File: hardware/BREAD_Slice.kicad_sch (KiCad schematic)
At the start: 60 parts, among them IC1 ADS131M08IPBS, J1 Conn_01x10_Female, J2 Screw_Term_01x04, J3 Screw_Term_01x04, J4 Screw_Term_01x04, J5 Screw_Term_01x04, J6 Screw_Term_01x04, J7 Screw_Term_01x04, J8 Screw_Term_01x04, J9 Screw_Term_01x04, U1 AP63205, U2 OP1177ARM, Y1 ACO-xxxMHz

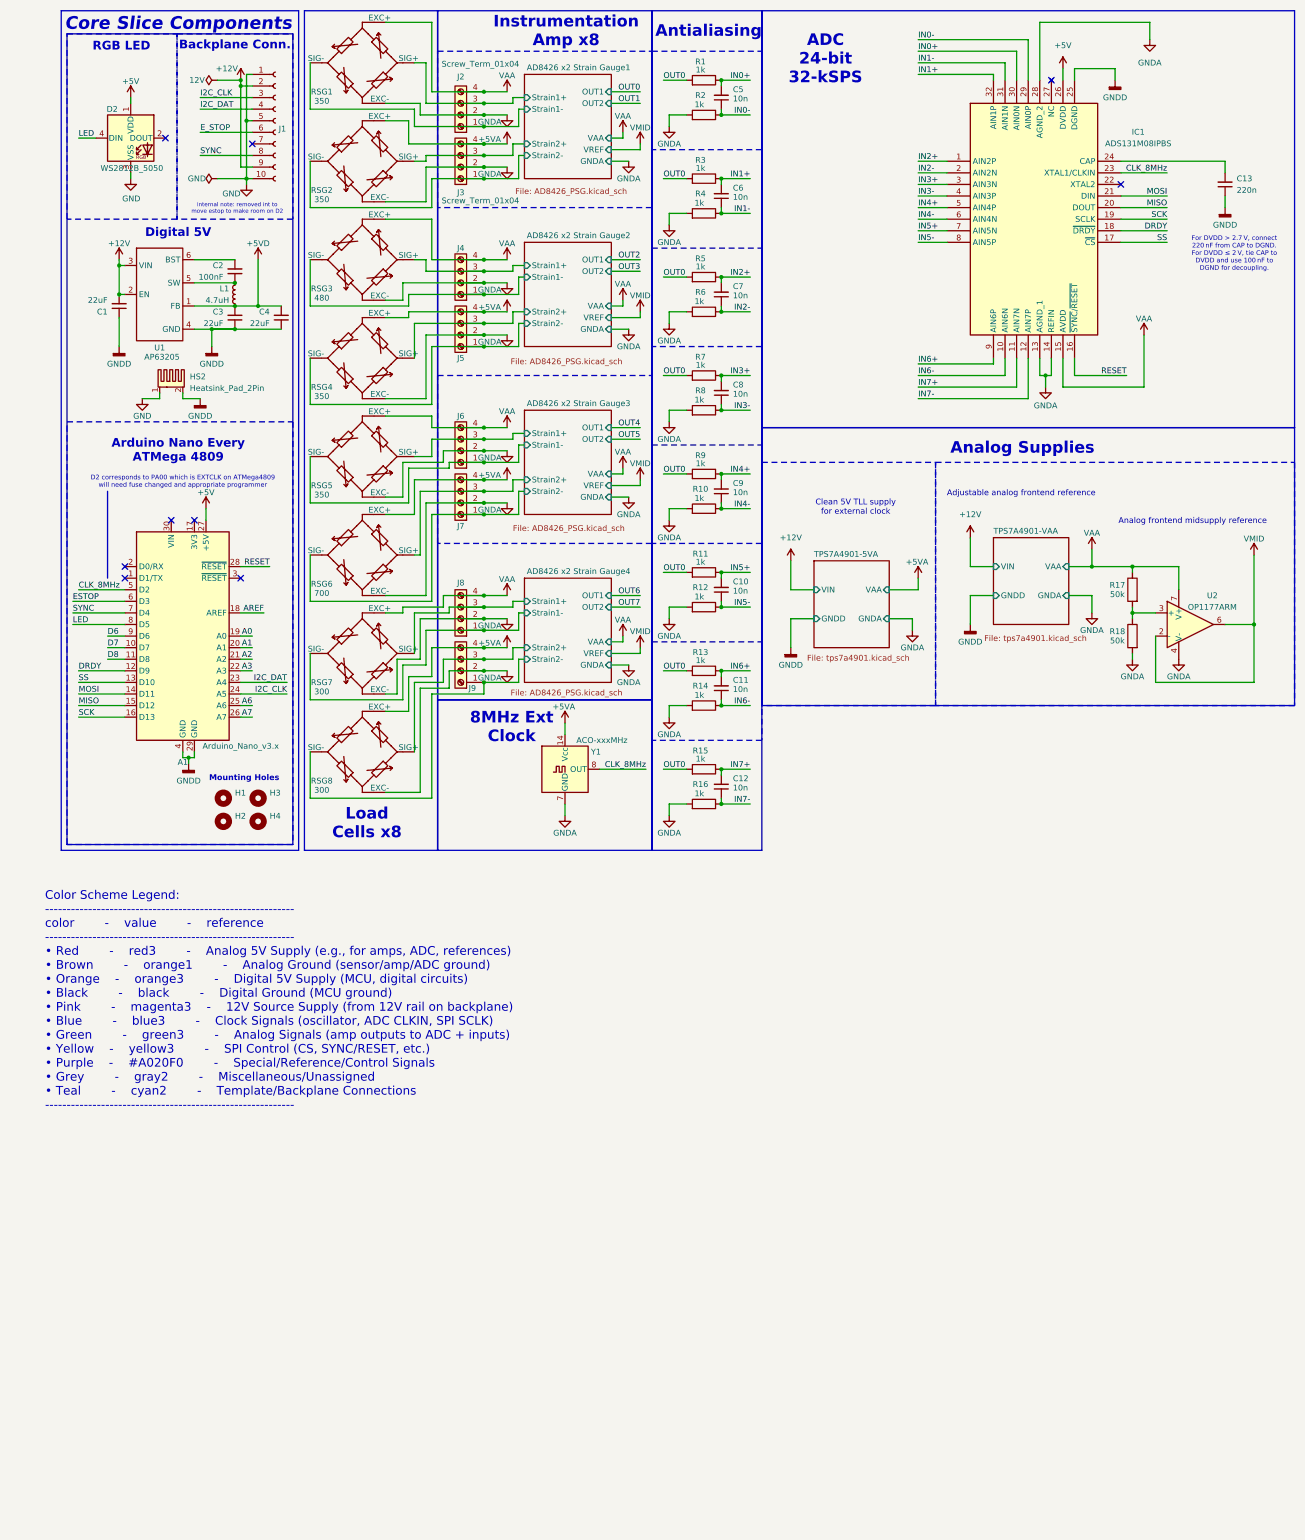
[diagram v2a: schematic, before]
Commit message: finalize board before switch to stm
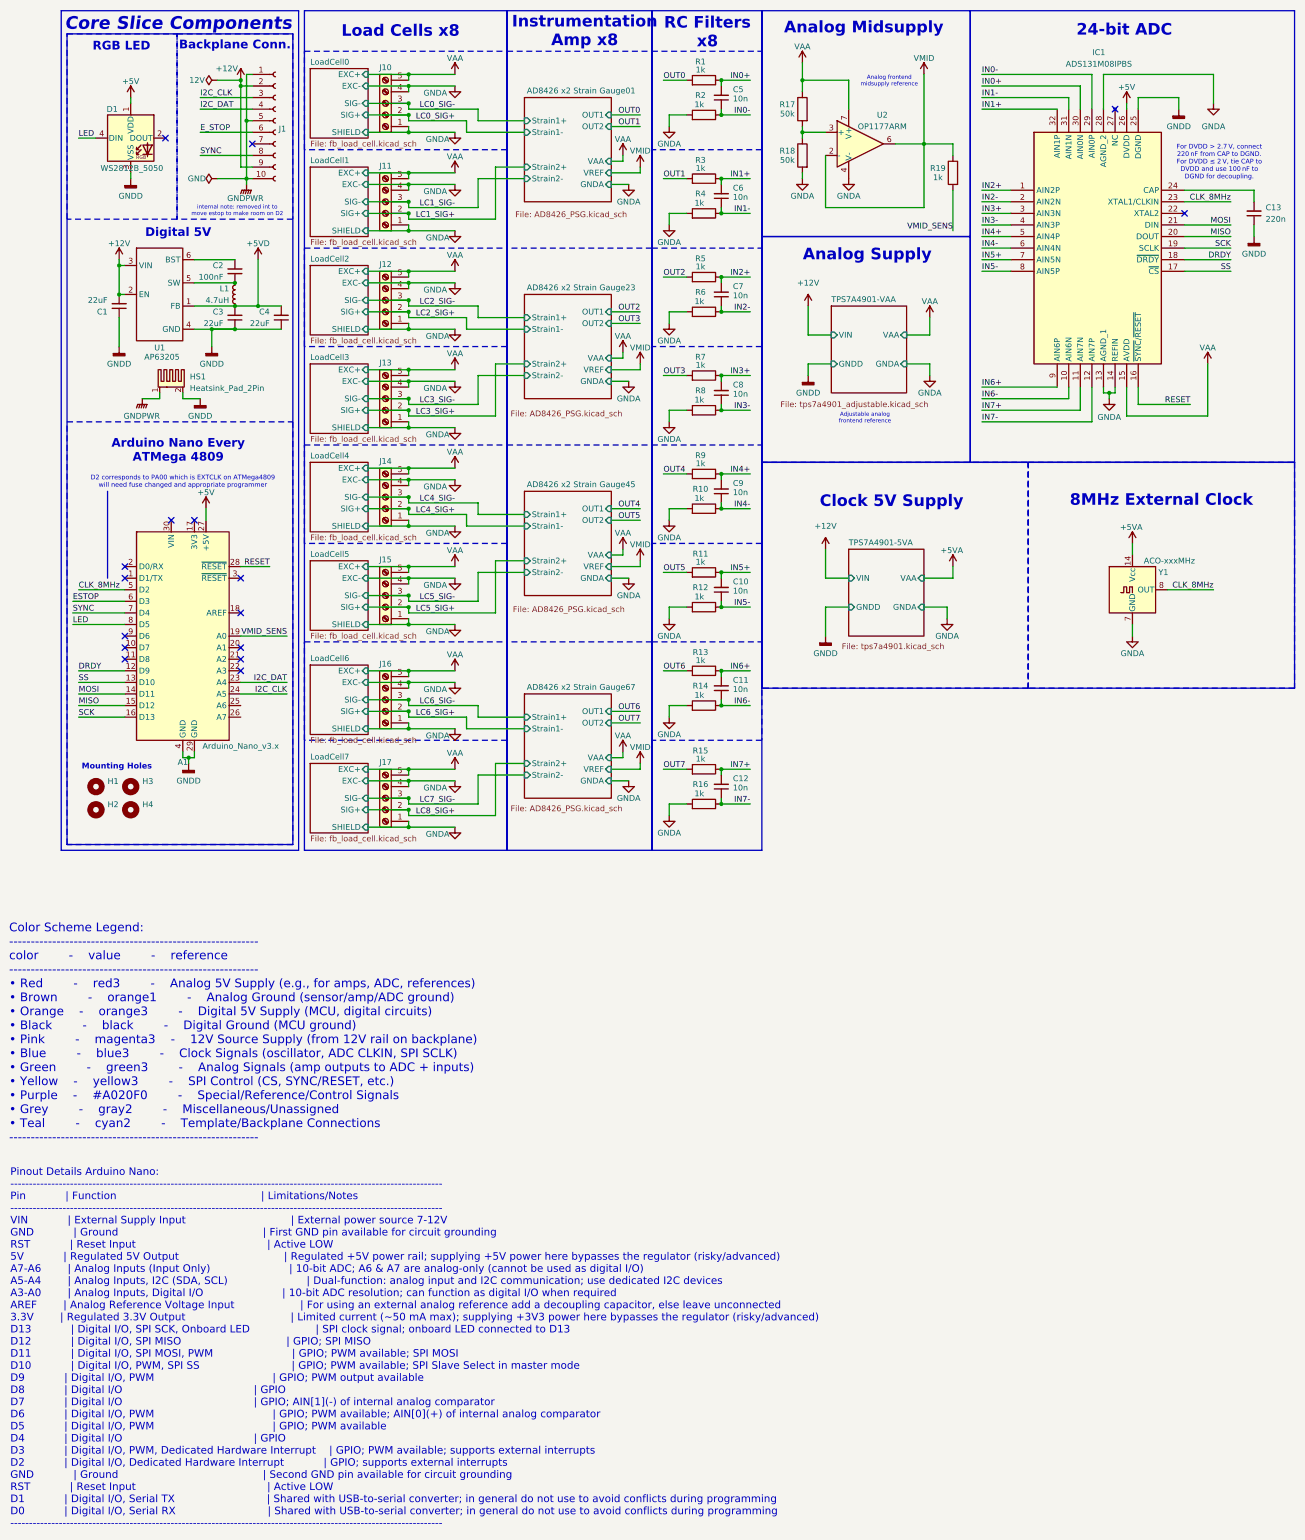
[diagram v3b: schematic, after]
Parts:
- removed J2, J3, J4, J5, J6, J7, J8, J9: Screw_Term_01x04, symbol Connector:Screw_Terminal_01x04
- removed RSG1, RSG2, RSG4, RSG5: 350, symbol kml-custom:Full Bridge Strain Gauge
- removed RSG3: 480, symbol kml-custom:Full Bridge Strain Gauge
- removed RSG6: 700, symbol kml-custom:Full Bridge Strain Gauge
- removed RSG7, RSG8: 300, symbol kml-custom:Full Bridge Strain Gauge
- added J10, J11, J12, J13, J14, J15, J16, J17: Screw_Terminal_01x05, TerminalBlock_4Ucon:TerminalBlock_4Ucon_1x05_P3.50mm_Horizontal, symbol Connector:Screw_Terminal_01x05
- added R19: 1k, symbol Device:R
- renumbered D2 to D1, HS2 to HS1
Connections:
- net GNDA: now also J10.1 (Pin_1), J10.4 (Pin_4), J11.1 (Pin_1), J11.4 (Pin_4), J12.1 (Pin_1), J12.4 (Pin_4), J13.1 (Pin_1), J13.4 (Pin_4), J14.1 (Pin_1), J14.4 (Pin_4), J15.1 (Pin_1), J15.4 (Pin_4), J16.1 (Pin_1), J16.4 (Pin_4), J17.1 (Pin_1), J17.4 (Pin_4)
- net GNDD: now also D1.3 (VSS)
- net OUT0: no longer R11.2, R13.2, R15.2, R3.2, R5.2, R7.2, R9.2
- net OUT1: now also R3.2
- net OUT2: now also R5.2
- net OUT3: now also R7.2
- net OUT4: now also R9.2
- net OUT5: now also R11.2
- net OUT6: now also R13.2
- net OUT7: now also R15.2
- net VAA: now also J10.5 (Pin_5), J11.5 (Pin_5), J12.5 (Pin_5), J13.5 (Pin_5), J14.5 (Pin_5), J15.5 (Pin_5), J16.5 (Pin_5), J17.5 (Pin_5)
- net VMID: now also R19.1
- net A0 renamed VMID_SENS
- net VMID_SENS: now also R19.2
- net A1: no longer names the net of A1.20 (A1)
- net A2: no longer names the net of A1.21 (A2)
- net A3: no longer names the net of A1.22 (A3)
- net A6: no longer names the net of A1.25 (A6)
- net A7: no longer names the net of A1.26 (A7)
- net AREF: no longer names the net of A1.18 (AREF)
- net D6: no longer names the net of A1.9 (D6)
- net D7: no longer names the net of A1.10 (D7)
- net D8: no longer names the net of A1.11 (D8)
- net GND renamed GNDPWR
- net GNDPWR: no longer D1.3 (VSS)
- new net LC0_SIG+: J10.2 (Pin_2)
- new net LC0_SIG-: J10.3 (Pin_3)
- new net LC1_SIG+: J11.2 (Pin_2)
- new net LC1_SIG-: J11.3 (Pin_3)
- new net LC2_SIG+: J12.2 (Pin_2)
- new net LC2_SIG-: J12.3 (Pin_3)
- new net LC3_SIG+: J13.2 (Pin_2)
- new net LC3_SIG-: J13.3 (Pin_3)
- new net LC4_SIG+: J14.2 (Pin_2)
- new net LC4_SIG-: J14.3 (Pin_3)
- new net LC5_SIG+: J15.2 (Pin_2)
- new net LC5_SIG-: J15.3 (Pin_3)
- new net LC6_SIG+: J16.2 (Pin_2)
- new net LC6_SIG-: J16.3 (Pin_3)
- new net LC7_SIG-: J17.3 (Pin_3)
- new net LC8_SIG+: J17.2 (Pin_2)
- no-connect marks 9 -> 16
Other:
- sheet AD8426 x2 Strain Gauge1 renamed AD8426 x2 Strain Gauge01
- sheet AD8426 x2 Strain Gauge2 renamed AD8426 x2 Strain Gauge23
- sheet AD8426 x2 Strain Gauge3 renamed AD8426 x2 Strain Gauge45
- sheet AD8426 x2 Strain Gauge4 renamed AD8426 x2 Strain Gauge67
- added sheet LoadCell0 (fb_load_cell.kicad_sch)
- added sheet LoadCell1 (fb_load_cell.kicad_sch)
- added sheet LoadCell2 (fb_load_cell.kicad_sch)
- added sheet LoadCell3 (fb_load_cell.kicad_sch)
- added sheet LoadCell4 (fb_load_cell.kicad_sch)
- added sheet LoadCell5 (fb_load_cell.kicad_sch)
- added sheet LoadCell6 (fb_load_cell.kicad_sch)
- added sheet LoadCell7 (fb_load_cell.kicad_sch)
- sheet TPS7A4901-VAA: file tps7a4901.kicad_sch -> tps7a4901_adjustable.kicad_sch
- note added: "24-bit ADC"
- note added: "8MHz External Clock"
- note added: "Analog Midsupply"
- note added: "Analog Supply"
- note added: "Clock 5V Supply"
- note added: "Pinout Details Arduino Nano: -------------------------------------------------------------------------------------------------------------------- Pin | Function | Limitations/Notes -------------------------------------------------------------------------------------------------------------------- VIN | External Supply Input | External power source 7-12V GND | Ground | First GND pin available for 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"
- note added: "RC Filters x8"
- note removed: "8MHz Ext Clock"
- note removed: "ADC 24-bit 32-kSPS"
- note removed: "Analog Supplies"
- note removed: "Antialiasing"
- note removed: "Clean 5V TLL supply for external clock"
- moved on the sheet: C13, H1, H2, H3, H4, IC1, R17, R18, U2, Y1

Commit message: final iteration of board with proper connectors and clean layout
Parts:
- removed A1: Arduino_Nano_v3.x, Module:Arduino_Nano, symbol MCU_Module:Arduino_Nano_v3.x
- removed HS1: Heatsink_Pad_2Pin, symbol Mechanical:Heatsink_Pad_2Pin
- removed J10, J11, J12, J13, J14, J15, J16, J17: Screw_Terminal_01x05, TerminalBlock_4Ucon:TerminalBlock_4Ucon_1x05_P3.50mm_Horizontal, symbol Connector:Screw_Terminal_01x05
- removed U2: OP1177ARM, Package_SO:MSOP-8_3x3mm_P0.65mm, symbol Amplifier_Operational:OP1177ARM
- removed Y1: ACO-xxxMHz, Oscillator:Oscillator_DIP-14, symbol Oscillator:ACO-xxxMHz
- added C13, C14: 1u, Capacitor_SMD:C_1206_3216Metric_Pad1.33x1.80mm_HandSolder, symbol Device:C_Small
- added HS1: Heatsink_Pad, kml-custom:Thermal Pad, symbol Mechanical:Heatsink_Pad
- added J10: Micro_SD_Card, Connector_Card:microSD_HC_Molex_47219-2001, symbol Connector:Micro_SD_Card
- added J2, J3, J4, J5, J6, J7, J8, J9: 1439890, 1439890, symbol kml-custom:1439890
- added NT1: NetTie_2, NetTie:NetTie-2_SMD_Pad2.0mm, symbol Device:NetTie_2
- added R20: 1k, Resistor_SMD:R_0805_2012Metric_Pad1.20x1.40mm_HandSolder, symbol Device:R
- added U2: NUCLEO-L432KC, kml-custom:MODULE_NUCLEO-L432KC, symbol kml-custom:NUCLEO-L432KC
- added U3: MCP6022, Package_SO:SOIC-8_3.9x4.9mm_P1.27mm, symbol Amplifier_Operational:MCP6022
- C10, C11, C12, C5, C6, C7, C8, C9: footprint Capacitor_SMD:C_1206_3216Metric -> Capacitor_SMD:C_0805_2012Metric_Pad1.18x1.45mm_HandSolder
- C15: renamed from C13; footprint Capacitor_SMD:C_1206_3216Metric -> Capacitor_SMD:C_1206_3216Metric_Pad1.33x1.80mm_HandSolder
- D1: footprint SparkFun-LED:WS2812-5050-4pin -> SparkFun-LED:WS2812-5050-4PIN
- IC1: footprint QFP50P700X700X120-32N -> kml-custom:QFP50P700X700X120-32N
- R1, R10, R11, R12, R13, R14, R15, R16, R19, R2, R3, R4, R5, R6, R7, R8, R9: footprint (none) -> Resistor_SMD:R_0805_2012Metric_Pad1.20x1.40mm_HandSolder
- R17, R18: value 50k -> 50k 1%; footprint (none) -> Resistor_SMD:R_0805_2012Metric_Pad1.20x1.40mm_HandSolder
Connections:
- net E_STOP is gone; now on net ESTOP: J1.6 (Pin_6)
- net +5VD: now also D1.1 (VDD), U2.CN4_4 (+5V), U3.8 (V+)
- net DRDY: now also U2.CN3_11 (PC15)
- net ESTOP: now also U2.CN3_5 (PA12)
- net GNDA: now also C14.1, J2.4, J2.5, J2.6, J3.4, J3.5, J3.6, J4.4, J4.5, J4.6, J5.4, J5.5, J5.6, J6.3, J6.5, J6.6, J7.3, J7.5, J7.6, J8.3, J8.5, J8.6, J9.3, J9.5, J9.6
- net GNDD: now also C13.1, HS1.1, J10.6 (VSS), J10.9 (SHIELD), NT1.2, U2.CN3_4 (GND_CN3), U2.CN4_2 (GND_CN4), U3.4 (V-)
- net GNDPWR: now also NT1.1
- net I2C_CLK: now also U2.CN4_7 (PA6)
- net I2C_DAT: now also U2.CN4_8 (PA5)
- net IN0+: now also IC1.29 (AIN0P); no longer IC1.30 (AIN0N)
- net IN0-: now also IC1.30 (AIN0N); no longer IC1.29 (AIN0P)
- net IN3+: now also IC1.4 (AIN3P); no longer IC1.3 (AIN3N)
- net IN3-: now also IC1.3 (AIN3N); no longer IC1.4 (AIN3P)
- net IN5+: now also IC1.8 (AIN5P); no longer IC1.7 (AIN5N)
- net IN5-: now also IC1.7 (AIN5N); no longer IC1.8 (AIN5P)
- net IN7+: now also IC1.12 (AIN7P); no longer IC1.11 (AIN7N)
- net IN7-: now also IC1.11 (AIN7N); no longer IC1.12 (AIN7P)
- net LC0_SIG+: now also J6.1
- net LC0_SIG-: now also J6.2
- net LC1_SIG+: now also J2.2
- net LC1_SIG-: now also J2.1
- net LC2_SIG+: now also J7.1
- net LC2_SIG-: now also J7.2
- net LC3_SIG+: now also J3.2
- net LC3_SIG-: now also J3.1
- net LC4_SIG+: now also J8.1
- net LC4_SIG-: now also J8.2
- net LC5_SIG+: now also J4.2
- net LC5_SIG-: now also J4.1
- net LC6_SIG+: now also J9.1
- net LC6_SIG-: now also J9.2
- net LC7_SIG-: now also J5.1
- net LED: now also U2.CN3_8 (PB6)
- net MISO: now also J10.7 (DAT0), U2.CN3_15 (PB4)
- net MOSI: now also J10.3 (CMD), U2.CN3_14 (PB5)
- net SCK: now also J10.5 (CLK), U2.CN4_15 (PB3)
- net SYNC: now also U2.CN3_7 (PB7)
- net VAA: now also J2.3, J3.3, J4.3, J5.3, J6.4, J7.4, J8.4, J9.4; no longer IC1.15 (AVDD)
- net VMID: now also U3.1, U3.2 (-)
- net VMID_SENS: now also U2.CN4_12 (PA0)
- net INT: now reaches J1.7 (Pin_7)
- net INT: now also U2.CN3_6 (PB0)
- net at R17.2, R18.1: now also U3.3 (+)
- net +5V renamed +3V3
- net +3V3: now also C13.2, J10.4 (VDD), U2.CN4_14 (+3V3); no longer D1.1 (VDD)
- net CLK_8MHz renamed CLK_MCO
- net CLK_MCO: now also U2.CN3_12 (PA8)
- net RESET renamed RST_ADC
- net RST_ADC: now also U2.CN3_10 (PC14)
- net SS renamed ADC_CS
- net ADC_CS: now also U2.CN3_9 (PB1)
- new net: R20.1, U3.6 (-), U3.7
- new net +3.3VADC: C14.2, IC1.15 (AVDD), U3.5 (+)
- new net LC7_SIG+: J5.2
- new net SD_CS: J10.2 (DAT3/CD), U2.CN3_13 (PA11)
- new net VADC_SENS: R20.2, U2.CN4_11 (PA1)
- no-connect marks 16 -> 20
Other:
- sheet AD8426 x2 Strain Gauge01 renamed AD8426 x2 StrainGauge01
- sheet AD8426 x2 Strain Gauge23 renamed AD8426 x2 StrainGauge23
- sheet AD8426 x2 Strain Gauge45 renamed AD8426 x2 StrainGauge45
- sheet AD8426 x2 Strain Gauge67 renamed AD8426 x2 StrainGauge67
- sheet TPS7A4901-5VA renamed TPS7A4901-3V3ADC
- sheet TPS7A4901-3V3ADC ports: added GND; removed GNDD
- sheet TPS7A4901-VAA ports: added GND; removed GNDD
- note added: "ADC 3V3 Supply"
- note added: "ADC Supply Sense Buffer"
- note added: "Analog Frontend 5-10V Supply"
- note added: "Analog Midsupply Reference"
- note added: "M12 Connectors"
- note added: "Pinout Details: STM32 Nucleo-32 L432KC ------------------------------------------------------------------------------------- Pin | Function | Notes ------------------------------------------------------------------------------------- VIN | External Supply Input | 7-12V input via CN4 pin 1; powers onboard 3.3V regulator GND | Ground | Ground reference (multiple available) NRST | Reset Input | Acti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"
- note added: "SB10 (VREF+) - ON: VREF+ on STM32 is connected to VDD. - OFF: VREF+ on STM32 is not connected to VDD and it is provided by pin 13 of CN4. SB15 (LD3-LED) - ON: Green user LED LD3 is connected to D13 of ARDUINO® Nano signal. - OFF: Green user LED LD3 is not connected. SB9 (NRST) - ON: The NRST signal of ST-LINK is connected to the NRST pin of the STM32. - OFF: The NRST signal of ST-LINK is not conn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"
- note added: "STM32 NUCLEO32 STM32L432KC"
- note removed: "8MHz External Clock"
- note removed: "Adjustable analog frontend reference"
- note removed: "Analog Midsupply"
- note removed: "Analog Supply"
- note removed: "Analog frontend midsupply reference"
- note removed: "Arduino Nano Every ATMega 4809"
- note removed: "Clock 5V Supply"
- note removed: "D2 corresponds to PA00 which is EXTCLK on ATMega4809 will need fuse changed and appropriate programmer"
- note removed: "Pinout Details Arduino Nano: -------------------------------------------------------------------------------------------------------------------- Pin | Function | Limitations/Notes -------------------------------------------------------------------------------------------------------------------- VIN | External Supply Input | External power source 7-12V GND | Ground | First GND pin available for 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"
- moved on the sheet: C10, C11, C12, C5, C6, C7, C8, C9, D1, H1, H2, H3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
